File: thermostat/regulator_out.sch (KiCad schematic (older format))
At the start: 29 parts, among them J3 Thermosthat - Molex PicoBlade, J6 Conn_02x02_Odd_Even, Q2 BSS806NL6327, Q6 BSS806NL6327, U5 LM2574M-5, U6 LD1117S33TR_SOT223, U7 LM358

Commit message: Replaced DCDC input cap as the package was way too small for the required capacitance, started working on the BOM and looking up parts on Mouser. Need to replace input Molex connector as it is not in stock at Mouser. Easiest is solder pads (I will have a connector on the other side of the cable anyway...) or just the same connector but with higher pincount that Mouser has in stock
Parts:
- removed R26: 0, Resistor_SMD:R_0603_1608Metric, symbol Device:R
- C32: footprint Capacitor_SMD:C_0805_2012Metric -> Capacitor_SMD:CP_Elec_6.3x3; symbol Device:C -> Device:C_Polarized
- C35: symbol Device:C -> Device:C_Polarized
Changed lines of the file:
@@
 $EndComp
 $Comp
-L Device:C C?
+L Device:C_Polarized C?
 U 1 1 5F453D8B
 P 1350 5250
@@
 F 0 "C32" H 1465 5296 50  0000 L CNN
 F 1 "22u" H 1465 5205 50  0000 L CNN
-F 2 "Capacitor_SMD:C_0805_2012Metric" H 1388 5100 50  0001 C CNN
+F 2 "Capacitor_SMD:CP_Elec_6.3x3" H 1388 5100 50  0001 C CNN
 F 3 "~" H 1350 5250 50  0001 C CNN
 	1    1350 5250
@@
 	3750 5300 3750 5250
 $Comp
-L Device:C C?
+L Device:C_Polarized C?
 U 1 1 5F453E2E
 P 3750 5450
@@
 $EndComp
 $Comp
-L Device:R R26
-U 1 1 5F7899BD
-P 7800 2200
-F 0 "R26" V 7593 2200 50  0000 C CNN
-F 1 "0" V 7684 2200 50  0000 C CNN
-F 2 "Resistor_SMD:R_0603_1608Metric" V 7730 2200 50  0001 C CNN
-F 3 "~" H 7800 2200 50  0001 C CNN
-	1    7800 2200
-	0    -1   -1   0
-$EndComp
-$Comp
 L power:GNDA #PWR016
 U 1 1 5F789E8B
@@
 $EndComp
 Wire Wire Line
-	8050 2400 8050 2200
-Wire Wire Line
-	8050 2200 7950 2200
-Connection ~ 8050 2200
-Wire Wire Line
-	8050 2200 8050 2150
-Wire Wire Line
-	7650 2200 7600 2200
-Wire Wire Line
-	7600 2200 7600 1950
-Wire Wire Line
 	7600 1950 7750 1950
 $Comp
@@
 Wire Wire Line
 	6750 1700 6750 1750
-Connection ~ 7600 1950
 Text Notes 6750 1000 0    50   ~ 0
 Double NMOS to counteract inverter
+Wire Wire Line
+	8050 2150 8050 2400
 $EndSCHEMATC

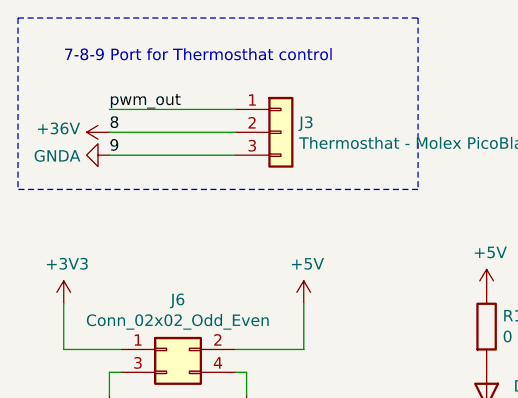
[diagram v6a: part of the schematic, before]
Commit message: Replaced Molex PicoBlade SMT connector with THT version as this is available at Mouser. This also helps since the pins act as vias. Resolved DRC errors, Antenna trace needs to be set then we are ready for production.
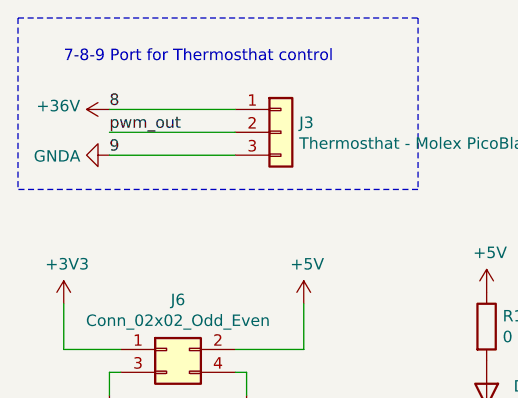
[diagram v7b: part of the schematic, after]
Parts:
- J3: footprint Connector_Molex:Molex_PicoBlade_53261-0371_1x03-1MP_P1.25mm_Horizontal -> Connector_Molex:Molex_PicoBlade_53048-0310_1x03_P1.25mm_Horizontal
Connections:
- net +36V: now also J3.1 (Pin_1); no longer J3.2 (Pin_2)
- net pwm_out: now also J3.2 (Pin_2); no longer J3.1 (Pin_1)
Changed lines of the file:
@@
 F 0 "J3" H 1830 1142 50  0000 L CNN
 F 1 "Thermosthat - Molex PicoBlade" H 1830 1051 50  0000 L CNN
-F 2 "Connector_Molex:Molex_PicoBlade_53261-0371_1x03-1MP_P1.25mm_Horizontal" H 1750 1100 50  0001 C CNN
+F 2 "Connector_Molex:Molex_PicoBlade_53048-0310_1x03_P1.25mm_Horizontal" H 1750 1100 50  0001 C CNN
 F 3 "Molex PicoBlade" H 1750 1100 50  0001 C CNN
 	1    1750 1100
 	1    0    0    -1
 $EndComp
-Text Label 1000 1100 0    50   ~ 0
+Text Label 1000 1000 0    50   ~ 0
 8
 Text Label 1000 1200 0    50   ~ 0
@@
 L power:+36V #PWR?
 U 1 1 5F3F4C34
-P 1000 1100
+P 1000 1000
 AR Path="/5F3F4C34" Ref="#PWR?"  Part="1"
 AR Path="/5E6A63AE/5F3F4C34" Ref="#PWR061"  Part="1"
-F 0 "#PWR061" H 1000 950 50  0001 C CNN
-F 1 "+36V" V 1015 1228 50  0000 L CNN
-F 2 "" H 1000 1100 50  0001 C CNN
-F 3 "" H 1000 1100 50  0001 C CNN
-	1    1000 1100
+F 0 "#PWR061" H 1000 850 50  0001 C CNN
+F 1 "+36V" V 1015 1128 50  0000 L CNN
+F 2 "" H 1000 1000 50  0001 C CNN
+F 3 "" H 1000 1000 50  0001 C CNN
+	1    1000 1000
 	0    -1   -1   0
 $EndComp
@@
 	1    0    0    -1
 $EndComp
-Text Label 1000 1000 0    50   ~ 0
+Text Label 1000 1100 0    50   ~ 0
 pwm_out
 Text HLabel 8650 4000 2    50   Input ~ 0

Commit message: Changed Button lines to MKW41 pins that also have LLWU interrupt capabilities. It will never get there, but who knows what the future brings.
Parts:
- C32, C35: symbol Device:C_Polarized -> home-thermostat-rescue:C_Polarized-Device
- L4: symbol Device:L_Iron -> home-thermostat-rescue:L_Iron-Device
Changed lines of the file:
@@
 $EndComp
 $Comp
-L Device:C_Polarized C?
+L home-thermostat-rescue:C_Polarized-Device C?
 U 1 1 5F453D8B
 P 1350 5250
@@
 $EndComp
 $Comp
-L Device:L_Iron L?
+L home-thermostat-rescue:L_Iron-Device L?
 U 1 1 5F453D97
 P 3400 5250
@@
 	3750 5300 3750 5250
 $Comp
-L Device:C_Polarized C?
+L home-thermostat-rescue:C_Polarized-Device C?
 U 1 1 5F453E2E
 P 3750 5450
